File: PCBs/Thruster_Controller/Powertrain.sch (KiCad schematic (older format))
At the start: 62 parts, among them Q1 SIZF906DT, Q2 SIZF906DT, Q3 SIZF906DT, U1 DRV8305

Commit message: More Layout and Routing
- Powertrain is mostly done, very tight and the phase and bus pads are sized and placed!
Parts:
- C17, C6, C7, C8: footprint Capacitors_SMD:C_0603 -> Capacitors_SMD:C_0402; Digikey 1276-CL10B104KB8NNNLCT-ND -> 490-10698-1-ND
- C24, C25, C26: footprint Capacitors_SMD:C_0603 -> Capacitors_SMD:C_0402; Digikey 490-1459-1-ND -> 490-6359-1-ND
- Q1, Q2, Q3: footprint MCU_Powertrain:SIZF906DT -> Thruster_Controller:SIZF906DT
- R12, R13, R14, R16: footprint Resistors_SMD:R_0603 -> Resistors_SMD:R_0402; Digikey P4.99KDBCT-ND -> 311-4.99KLRCT-ND
- R15, R3, R4, R5: footprint Resistors_SMD:R_0603 -> Resistors_SMD:R_0402; Digikey P22KDBCT-ND -> RMCF0402FT22K0CT-ND
- R20, R21, R22: footprint Resistors_SMD:R_0603 -> Resistors_SMD:R_0402; Digikey A129673CT-ND -> 311-56JRCT-ND
- U1: footprint MCU_Powertrain:DRV8305 -> Thruster_Controller:DRV8305
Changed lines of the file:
@@
 F 0 "U1" H 2575 5706 79  0000 C CNN
 F 1 "DRV8305" H 2575 5571 79  0000 C CNN
-F 2 "MCU_Powertrain:DRV8305" H 2500 3825 79  0001 C CNN
+F 2 "Thruster_Controller:DRV8305" H 2500 3825 79  0001 C CNN
 F 3 "http://www.ti.com/lit/ds/symlink/drv8305.pdf" H 4950 5425 79  0001 C CNN
 F 4 "296-42659-1-ND" H 4100 5275 79  0001 C CNN "Digikey"
@@
 F 0 "C26" H 1725 6475 50  0000 L CNN
 F 1 "2200pF" H 1600 6325 50  0000 L CNN
-F 2 "Capacitors_SMD:C_0603" H 1900 6400 50  0001 C CNN
+F 2 "Capacitors_SMD:C_0402" H 1900 6400 50  0001 C CNN
 F 3 "" H 1900 6400 50  0001 C CNN
-F 4 "490-1459-1-ND" H 1900 6400 50  0001 C CNN "Digikey"
+F 4 "490-6359-1-ND" H 1900 6400 50  0001 C CNN "Digikey"
 	1    1900 6400
 	1    0    0    -1
@@
 F 0 "R20" V 2075 5800 50  0000 C CNN
 F 1 "56" V 2075 6150 50  0000 C CNN
-F 2 "Resistors_SMD:R_0603" V 2165 5965 50  0001 C CNN
+F 2 "Resistors_SMD:R_0402" V 2165 5965 50  0001 C CNN
 F 3 "~" H 2125 5975 50  0001 C CNN
-F 4 "A129673CT-ND" V 2125 5975 50  0001 C CNN "Digikey"
+F 4 "311-56JRCT-ND" V 2125 5975 50  0001 C CNN "Digikey"
 	1    2125 5975
 	0    1    1    0
@@
 F 0 "R16" H 9185 4005 50  0000 L CNN
 F 1 "4.99k" H 9185 3930 50  0000 L CNN
-F 2 "Resistors_SMD:R_0603" V 9175 3995 50  0001 C CNN
+F 2 "Resistors_SMD:R_0402" V 9175 3995 50  0001 C CNN
 F 3 "~" H 9135 4005 50  0001 C CNN
-F 4 "P4.99KDBCT-ND" H 9135 4005 50  0001 C CNN "Digikey"
+F 4 "311-4.99KLRCT-ND" H 9135 4005 50  0001 C CNN "Digikey"
 	1    9135 4005
 	1    0    0    -1
@@
 F 0 "C17" H 9585 4055 50  0000 L CNN
 F 1 "0.1uF" H 9585 3980 50  0000 L CNN
-F 2 "Capacitors_SMD:C_0603" H 9510 4005 50  0001 C CNN
+F 2 "Capacitors_SMD:C_0402" H 9510 4005 50  0001 C CNN
 F 3 "" H 9510 4005 50  0001 C CNN
-F 4 "1276-CL10B104KB8NNNLCT-ND" H 9510 4005 50  0001 C CNN "Digikey"
+F 4 "490-10698-1-ND" H 9510 4005 50  0001 C CNN "Digikey"
 	1    9510 4005
 	1    0    0    -1
@@
 F 0 "Q3" H 6225 1600 50  0000 L CNN
 F 1 "SIZF906DT" H 6225 1525 50  0000 L CNN
-F 2 "MCU_Powertrain:SIZF906DT" H 6200 1575 50  0001 C CNN
+F 2 "Thruster_Controller:SIZF906DT" H 6200 1575 50  0001 C CNN
 F 3 "http://www.vishay.com/docs/67547/sizf906dt.pdf" H 6000 1475 50  0001 C CNN
 F 4 "SIZF906DT-T1-GE3CT-ND" H 6000 1425 50  0001 C CNN "Digikey"
@@
 F 0 "R5" H 6543 2171 50  0000 L CNN
 F 1 "22.0k" H 6543 2080 50  0000 L CNN
-F 2 "Resistors_SMD:R_0603" V 6515 2115 50  0001 C CNN
+F 2 "Resistors_SMD:R_0402" V 6515 2115 50  0001 C CNN
 F 3 "~" H 6475 2125 50  0001 C CNN
-F 4 "P22KDBCT-ND" H 6475 2125 50  0001 C CNN "Digikey"
+F 4 "RMCF0402FT22K0CT-ND" H 6475 2125 50  0001 C CNN "Digikey"
 	1    6475 2125
 	1    0    0    -1
@@
 F 0 "R14" H 6525 2525 50  0000 L CNN
 F 1 "4.99k" H 6525 2450 50  0000 L CNN
-F 2 "Resistors_SMD:R_0603" V 6515 2515 50  0001 C CNN
+F 2 "Resistors_SMD:R_0402" V 6515 2515 50  0001 C CNN
 F 3 "~" H 6475 2525 50  0001 C CNN
-F 4 "P4.99KDBCT-ND" H 6475 2525 50  0001 C CNN "Digikey"
+F 4 "311-4.99KLRCT-ND" H 6475 2525 50  0001 C CNN "Digikey"
 	1    6475 2525
 	1    0    0    -1
@@
 F 0 "Q1" H 8175 1600 50  0000 L CNN
 F 1 "SIZF906DT" H 8175 1525 50  0000 L CNN
-F 2 "MCU_Powertrain:SIZF906DT" H 8150 1575 50  0001 C CNN
+F 2 "Thruster_Controller:SIZF906DT" H 8150 1575 50  0001 C CNN
 F 3 "http://www.vishay.com/docs/67547/sizf906dt.pdf" H 7950 1475 50  0001 C CNN
 F 4 "SIZF906DT-T1-GE3CT-ND" H 7950 1425 50  0001 C CNN "Digikey"
@@
 F 0 "R12" H 8475 2525 50  0000 L CNN
 F 1 "4.99k" H 8475 2450 50  0000 L CNN
-F 2 "Resistors_SMD:R_0603" V 8465 2515 50  0001 C CNN
+F 2 "Resistors_SMD:R_0402" V 8465 2515 50  0001 C CNN
 F 3 "~" H 8425 2525 50  0001 C CNN
-F 4 "P4.99KDBCT-ND" H 8425 2525 50  0001 C CNN "Digikey"
+F 4 "311-4.99KLRCT-ND" H 8425 2525 50  0001 C CNN "Digikey"
 	1    8425 2525
 	1    0    0    -1
@@
 F 0 "Q2" H 10070 1595 50  0000 L CNN
 F 1 "SIZF906DT" H 10070 1520 50  0000 L CNN
-F 2 "MCU_Powertrain:SIZF906DT" H 10045 1570 50  0001 C CNN
+F 2 "Thruster_Controller:SIZF906DT" H 10045 1570 50  0001 C CNN
 F 3 "http://www.vishay.com/docs/67547/sizf906dt.pdf" H 9845 1470 50  0001 C CNN
 F 4 "SIZF906DT-T1-GE3CT-ND" H 9845 1420 50  0001 C CNN "Digikey"
@@
 F 0 "R13" H 10370 2520 50  0000 L CNN
 F 1 "4.99k" H 10370 2445 50  0000 L CNN
-F 2 "Resistors_SMD:R_0603" V 10360 2510 50  0001 C CNN
+F 2 "Resistors_SMD:R_0402" V 10360 2510 50  0001 C CNN
 F 3 "~" H 10320 2520 50  0001 C CNN
-F 4 "P4.99KDBCT-ND" H 10320 2520 50  0001 C CNN "Digikey"
+F 4 "311-4.99KLRCT-ND" H 10320 2520 50  0001 C CNN "Digikey"
 	1    10320 2520
 	1    0    0    -1
@@
 F 0 "C25" H 1400 6475 50  0000 L CNN
 F 1 "2200pF" H 1275 6325 50  0000 L CNN
-F 2 "Capacitors_SMD:C_0603" H 1575 6400 50  0001 C CNN
+F 2 "Capacitors_SMD:C_0402" H 1575 6400 50  0001 C CNN
 F 3 "" H 1575 6400 50  0001 C CNN
-F 4 "490-1459-1-ND" H 1575 6400 50  0001 C CNN "Digikey"
+F 4 "490-6359-1-ND" H 1575 6400 50  0001 C CNN "Digikey"
 	1    1575 6400
 	1    0    0    -1
@@
 F 0 "C24" H 1075 6475 50  0000 L CNN
 F 1 "2200pF" H 950 6325 50  0000 L CNN
-F 2 "Capacitors_SMD:C_0603" H 1250 6400 50  0001 C CNN
+F 2 "Capacitors_SMD:C_0402" H 1250 6400 50  0001 C CNN
 F 3 "" H 1250 6400 50  0001 C CNN
-F 4 "490-1459-1-ND" H 1250 6400 50  0001 C CNN "Digikey"
+F 4 "490-6359-1-ND" H 1250 6400 50  0001 C CNN "Digikey"
 	1    1250 6400
 	1    0    0    -1
@@
 F 0 "C8" H 6975 2575 50  0000 L CNN
 F 1 "0.1uF" H 6975 2500 50  0000 L CNN
-F 2 "Capacitors_SMD:C_0603" H 6900 2525 50  0001 C CNN
+F 2 "Capacitors_SMD:C_0402" H 6900 2525 50  0001 C CNN
 F 3 "" H 6900 2525 50  0001 C CNN
-F 4 "1276-CL10B104KB8NNNLCT-ND" H 6900 2525 50  0001 C CNN "Digikey"
+F 4 "490-10698-1-ND" H 6900 2525 50  0001 C CNN "Digikey"
 	1    6900 2525
 	1    0    0    -1
@@
 F 0 "C6" H 8925 2575 50  0000 L CNN
 F 1 "0.1uF" H 8925 2500 50  0000 L CNN
-F 2 "Capacitors_SMD:C_0603" H 8850 2525 50  0001 C CNN
+F 2 "Capacitors_SMD:C_0402" H 8850 2525 50  0001 C CNN
 F 3 "" H 8850 2525 50  0001 C CNN
-F 4 "1276-CL10B104KB8NNNLCT-ND" H 8850 2525 50  0001 C CNN "Digikey"
+F 4 "490-10698-1-ND" H 8850 2525 50  0001 C CNN "Digikey"
 	1    8850 2525
 	1    0    0    -1
@@
 F 0 "C7" H 10820 2570 50  0000 L CNN
 F 1 "0.1uF" H 10820 2495 50  0000 L CNN
-F 2 "Capacitors_SMD:C_0603" H 10745 2520 50  0001 C CNN
+F 2 "Capacitors_SMD:C_0402" H 10745 2520 50  0001 C CNN
 F 3 "" H 10745 2520 50  0001 C CNN
-F 4 "1276-CL10B104KB8NNNLCT-ND" H 10745 2520 50  0001 C CNN "Digikey"
+F 4 "490-10698-1-ND" H 10745 2520 50  0001 C CNN "Digikey"
 	1    10745 2520
 	1    0    0    -1
@@
 F 0 "R21" V 2075 5900 50  0000 C CNN
 F 1 "56" V 2075 6250 50  0000 C CNN
-F 2 "Resistors_SMD:R_0603" V 2165 6065 50  0001 C CNN
+F 2 "Resistors_SMD:R_0402" V 2165 6065 50  0001 C CNN
 F 3 "~" H 2125 6075 50  0001 C CNN
-F 4 "A129673CT-ND" V 2125 6075 50  0001 C CNN "Digikey"
+F 4 "311-56JRCT-ND" V 2125 6075 50  0001 C CNN "Digikey"
 	1    2125 6075
 	0    1    1    0
@@
 F 0 "R22" V 2075 6000 50  0000 C CNN
 F 1 "56" V 2075 6350 50  0000 C CNN
-F 2 "Resistors_SMD:R_0603" V 2165 6165 50  0001 C CNN
+F 2 "Resistors_SMD:R_0402" V 2165 6165 50  0001 C CNN
 F 3 "~" H 2125 6175 50  0001 C CNN
-F 4 "A129673CT-ND" V 2125 6175 50  0001 C CNN "Digikey"
+F 4 "311-56JRCT-ND" V 2125 6175 50  0001 C CNN "Digikey"
 	1    2125 6175
 	0    1    1    0
@@
 F 0 "R3" H 8493 2171 50  0000 L CNN
 F 1 "22.0k" H 8493 2080 50  0000 L CNN
-F 2 "Resistors_SMD:R_0603" V 8465 2115 50  0001 C CNN
+F 2 "Resistors_SMD:R_0402" V 8465 2115 50  0001 C CNN
 F 3 "~" H 8425 2125 50  0001 C CNN
-F 4 "P22KDBCT-ND" H 8425 2125 50  0001 C CNN "Digikey"
+F 4 "RMCF0402FT22K0CT-ND" H 8425 2125 50  0001 C CNN "Digikey"
 	1    8425 2125
 	1    0    0    -1
@@
 F 0 "R4" H 10388 2166 50  0000 L CNN
 F 1 "22.0k" H 10388 2075 50  0000 L CNN
-F 2 "Resistors_SMD:R_0603" V 10360 2110 50  0001 C CNN
+F 2 "Resistors_SMD:R_0402" V 10360 2110 50  0001 C CNN
 F 3 "~" H 10320 2120 50  0001 C CNN
-F 4 "P22KDBCT-ND" H 10320 2120 50  0001 C CNN "Digikey"
+F 4 "RMCF0402FT22K0CT-ND" H 10320 2120 50  0001 C CNN "Digikey"
 	1    10320 2120
 	1    0    0    -1
@@
 F 0 "R15" H 9203 3651 50  0000 L CNN
 F 1 "22.0k" H 9203 3560 50  0000 L CNN
-F 2 "Resistors_SMD:R_0603" V 9175 3595 50  0001 C CNN
+F 2 "Resistors_SMD:R_0402" V 9175 3595 50  0001 C CNN
 F 3 "~" H 9135 3605 50  0001 C CNN
-F 4 "P22KDBCT-ND" H 9135 3605 50  0001 C CNN "Digikey"
+F 4 "RMCF0402FT22K0CT-ND" H 9135 3605 50  0001 C CNN "Digikey"
 	1    9135 3605
 	1    0    0    -1

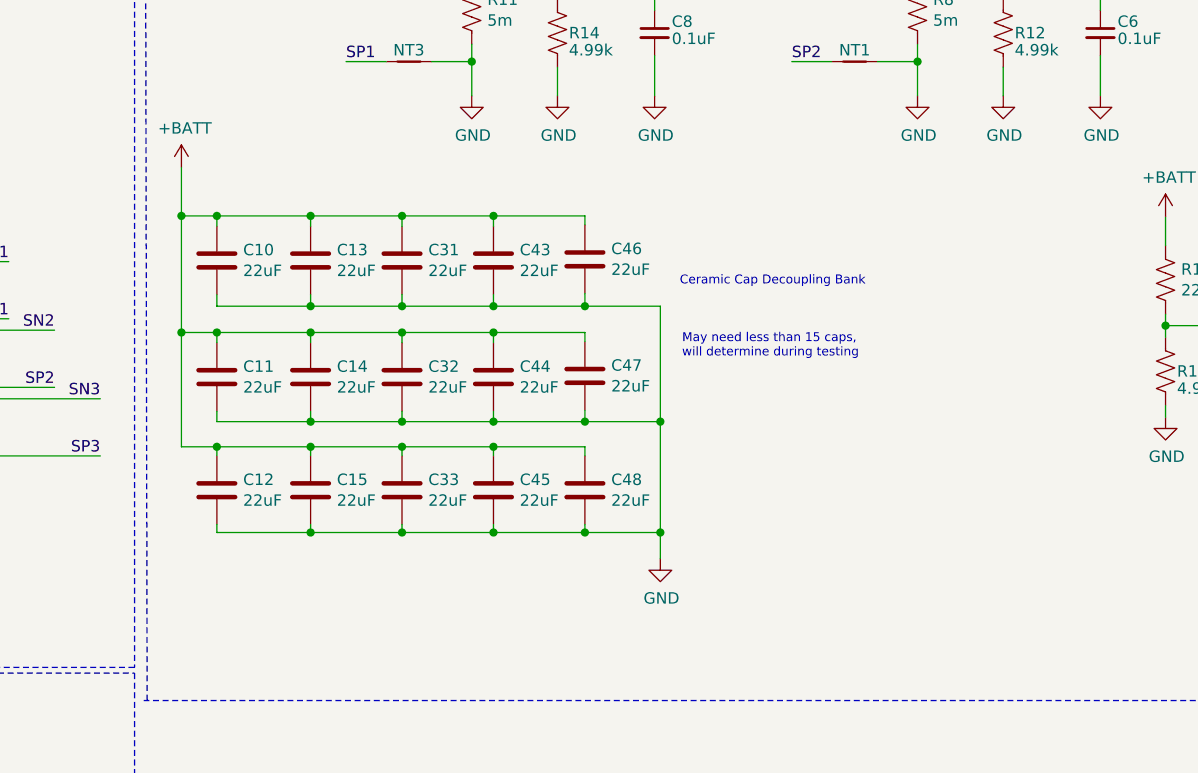
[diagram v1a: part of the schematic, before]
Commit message: Silk and Routing
- Fixed 5V LED indicator
- Small layout and routing cleanups
- Cleaned up Silkscreen
- Board is "finished" !!
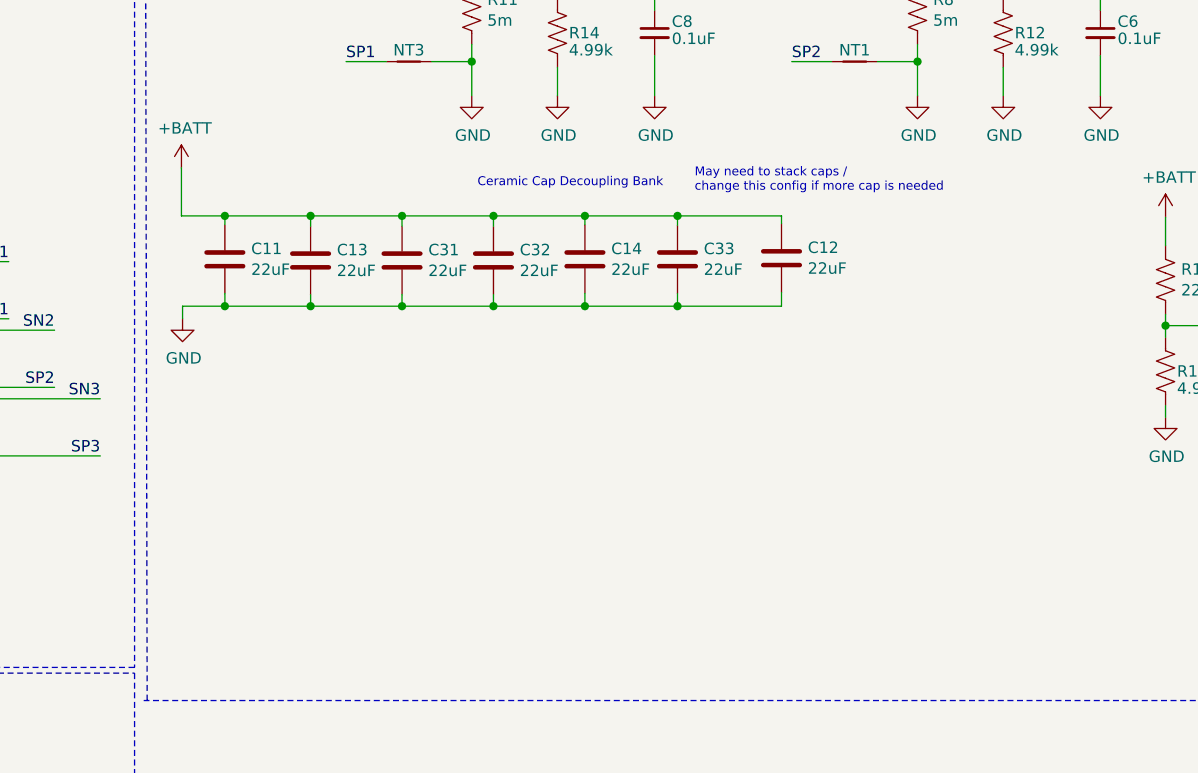
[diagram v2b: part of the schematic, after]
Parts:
- removed C10, C15, C43, C44, C45, C46, C47, C48: 22uF, Capacitors_SMD:C_1812, symbol Device:C
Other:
- note added: "May need to stack caps / \nchange this config if more cap is needed"
- note removed: "May need less than 15 caps,\nwill determine during testing"
- moved on the sheet: C11, C12, C14, C32, C33

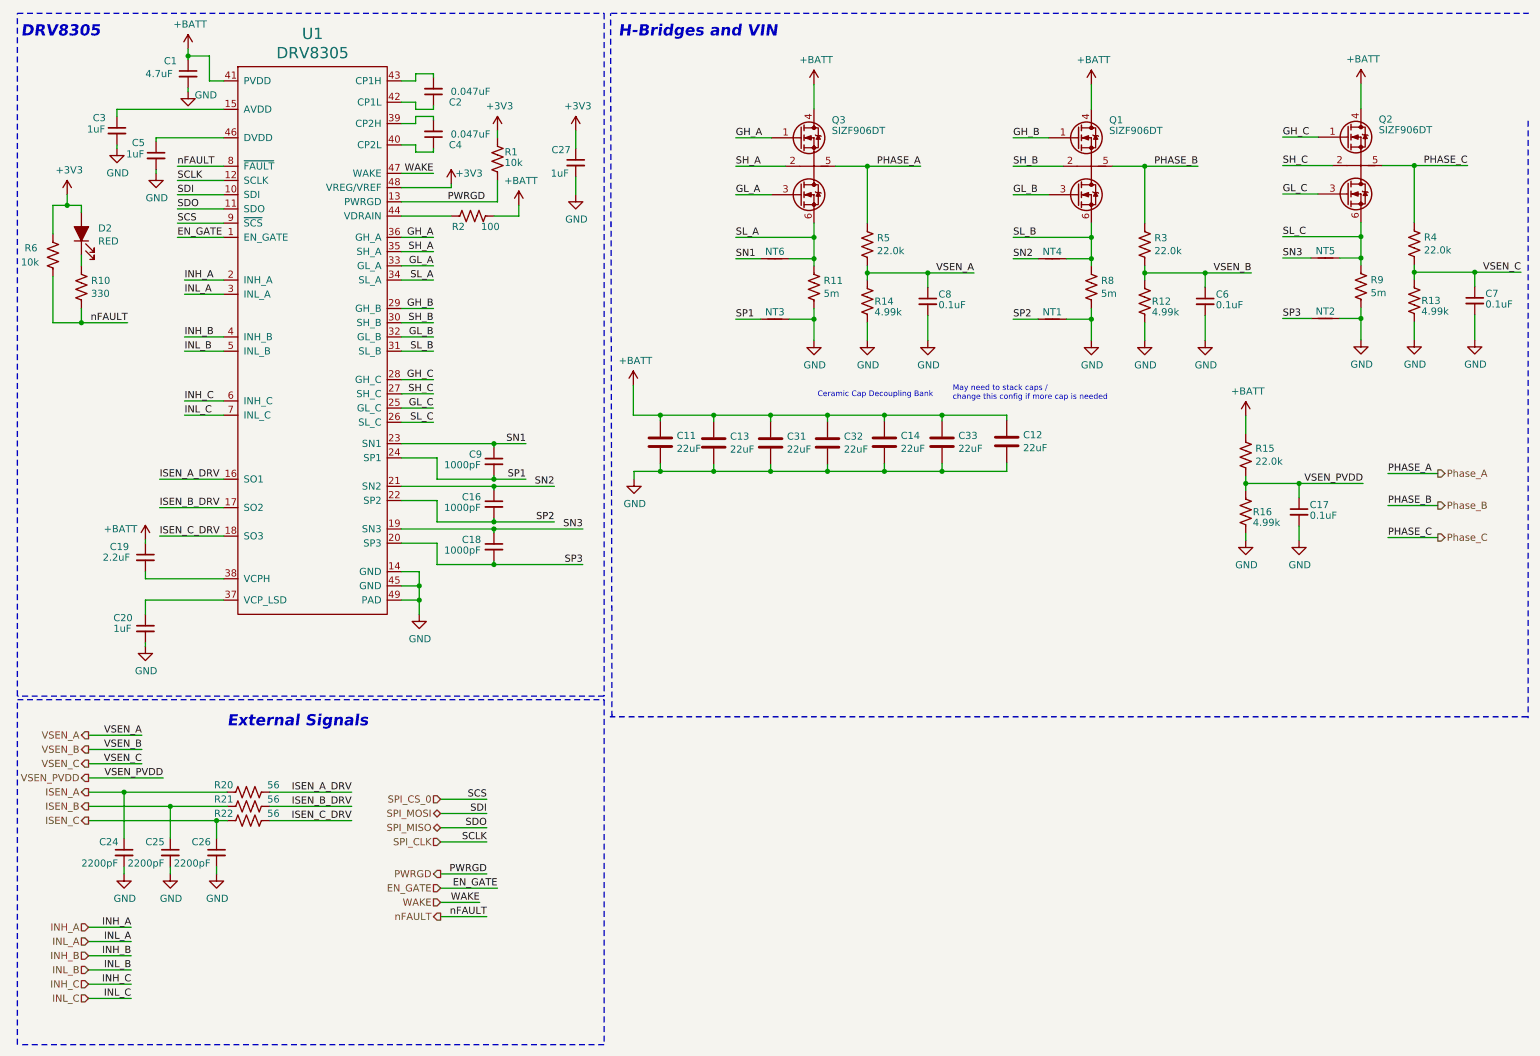
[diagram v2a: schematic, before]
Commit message: BOM and Small Changes
- Created BOM
- Small routing cleanups
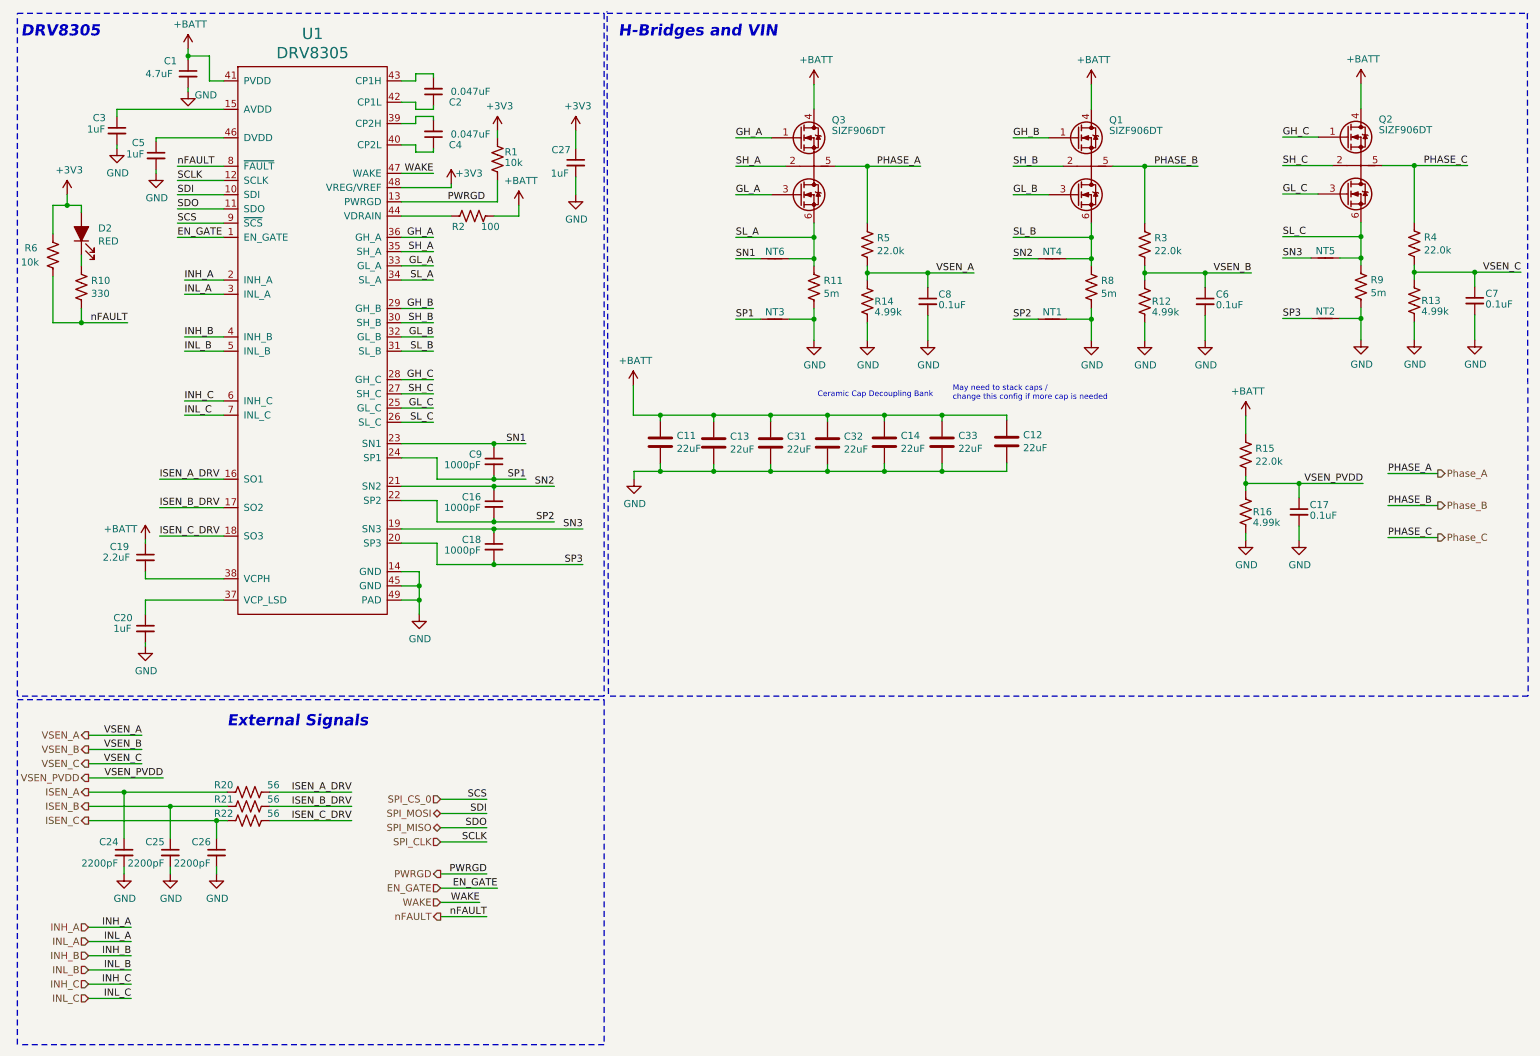
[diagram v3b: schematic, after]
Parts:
- D2: Digikey 160-1447-1-ND -> 732-4978-1-ND
- R1, R6: Digikey RNCP0603FTD10K0CT-ND -> RMCF0603JT10K0CT-ND
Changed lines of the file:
@@
 F 2 "LEDs:LED_0603" H 950 2050 50  0001 C CNN
 F 3 "~" H 950 2050 50  0001 C CNN
-F 4 "160-1447-1-ND" V 950 2050 50  0001 C CNN "Digikey"
+F 4 "732-4978-1-ND" V 950 2050 50  0001 C CNN "Digikey"
 	1    950  2050
 	0    -1   -1   0
@@
 F 2 "Resistors_SMD:R_0603" V 790 2190 50  0001 C CNN
 F 3 "~" H 750 2200 50  0001 C CNN
-F 4 "RNCP0603FTD10K0CT-ND" H 750 2200 50  0001 C CNN "Digikey"
+F 4 "RMCF0603JT10K0CT-ND" H 750 2200 50  0001 C CNN "Digikey"
 	1    750  2200
 	1    0    0    -1
@@
 F 2 "Resistors_SMD:R_0603" V 3915 1515 50  0001 C CNN
 F 3 "~" H 3875 1525 50  0001 C CNN
-F 4 "RNCP0603FTD10K0CT-ND" H 3875 1525 50  0001 C CNN "Digikey"
+F 4 "RMCF0603JT10K0CT-ND" H 3875 1525 50  0001 C CNN "Digikey"
 	1    3875 1525
 	1    0    0    -1
@@
 	500  5300 500  500
 Wire Notes Line
-	4675 500  11125 500
+	4645 500  11125 500
 Wire Notes Line
-	11120 1255 11120 5455
+	11115 500  11120 5300
 Wire Notes Line
-	11115 5445 4665 5445
+	11120 5300 4645 5300
 Wire Notes Line
-	4680 5445 4670 500
+	4655 5285 4645 485
 Wire Notes Line
 	4625 7750 525  7750
